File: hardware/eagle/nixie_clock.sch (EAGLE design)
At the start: 67 parts, among them IC1 74141N, IC10 7477N, IC11 74141N, IC12 7477N, IC13 74AC11238, IC2 7477N, IC3 74141N, IC4 7477N, IC5 74141N, IC6 7477N, IC7 74141N, IC8 7477N, IC9 74141N, J1_180V 22-27-2021-02, J1_5V1 22-27-2021-02, J1_5V2 22-27-2021-02, K1 4052, SW1 ROTARTY_ENCODER

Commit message: Working on Sunday
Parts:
- removed Q1: (no value), SparkFun-DiscreteSemi:TRANSISTOR_NPN2N3904
- added C16: 100nF, resistor:C-EU025-024X044
- added D1: LED-RGB-CA-THRUCLEAR, SparkFun-LED:LED-RGB-CA-THRUCLEAR
- added ULN1: (no value), SparkFun-PowerIC:ULN2803DIP
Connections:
- removed net N$124: C1.2, C10.2, C11.2, C12.2, C13.2, C2.2, C3.2, C4.2, C5.2, C6.2, C7.2, C8.2, C9.2, IC10P.VCC, IC11P.VCC, IC12P.VCC, IC13A.G1, IC13P.VCC, IC1P.VCC, IC2P.VCC, IC3P.VCC, IC4P.VCC, IC5P.VCC, IC6P.VCC, IC7P.VCC, IC8P.VCC, IC9P.VCC, J1_5V1-2.S, Q1.C
- new net N$138: GPIO_HEADER1G$1.GPIO$15, ULN1.2
- new net N$139: GPIO_HEADER1G$1.GPIO$16, ULN1.3
- new net N$140: C1.2, C10.2, C11.2, C12.2, C13.2, C16.2, C2.2, C3.2, C4.2, C5.2, C6.2, C7.2, C8.2, C9.2, IC10P.VCC, IC11P.VCC, IC12P.VCC, IC13A.G1, IC13P.VCC, IC1P.VCC, IC2P.VCC, IC3P.VCC, IC4P.VCC, IC5P.VCC, IC6P.VCC, IC7P.VCC, IC8P.VCC, IC9P.VCC, J1_5V1-2.S, ULN1.10
- net GND: now also C16.1, ULN1.9
- net N$137: now also ULN1.1; no longer Q1.B
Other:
- moved on the sheet: SV15, SW1

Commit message: Added uln documentation
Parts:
- removed GPIO_HEADER1: RPI_GPIO_HEADER, rpi-header:RPI_GPIO_HEADER
- added J1: RASPBERRYPI-40-PIN-GPIO, SparkFun-Boards:RASPBERRYPI-40-PIN-GPIO
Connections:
- removed net N$135: GPIO_HEADER1G$1.GPIO$11, SV16.5
- removed net N$136: GPIO_HEADER1G$1.GPIO$13, SV16.3
- new net N$124: J1.CE1, SV16.5
- net N$127: now also J1.MOSI; no longer GPIO_HEADER1G$1.GPIO$12
- net N$129: now also J1.GP4; no longer GPIO_HEADER1G$1.GPIO$7
- net N$130: now also J1.MISO, SV16.3; no longer GPIO_HEADER1G$1.GPIO$10
- net N$137: now also J1.SCLK; no longer GPIO_HEADER1G$1.GPIO$14
- net N$138: now also J1.TXO; no longer GPIO_HEADER1G$1.GPIO$15
- net N$139: now also J1.RXI; no longer GPIO_HEADER1G$1.GPIO$16
- net N$17: now also J1.GP22; no longer GPIO_HEADER1G$1.GPIO$3
- net N$94: now also J1.GP23; no longer GPIO_HEADER1G$1.GPIO$4
- net N$95: now also J1.GP24; no longer GPIO_HEADER1G$1.GPIO$5
- net N$96: now also J1.GP25; no longer GPIO_HEADER1G$1.GPIO$6
- net N$97: now also J1.GP27; no longer GPIO_HEADER1G$1.GPIO$2
- net N$98: now also J1.GP18#; no longer GPIO_HEADER1G$1.GPIO$1
- net N$99: now also J1.GP17; no longer GPIO_HEADER1G$1.GPIO$0
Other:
- moved on the sheet: B1, C1, C10, C11, C12, C13, C14, C15, C16, C2, C3, C4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

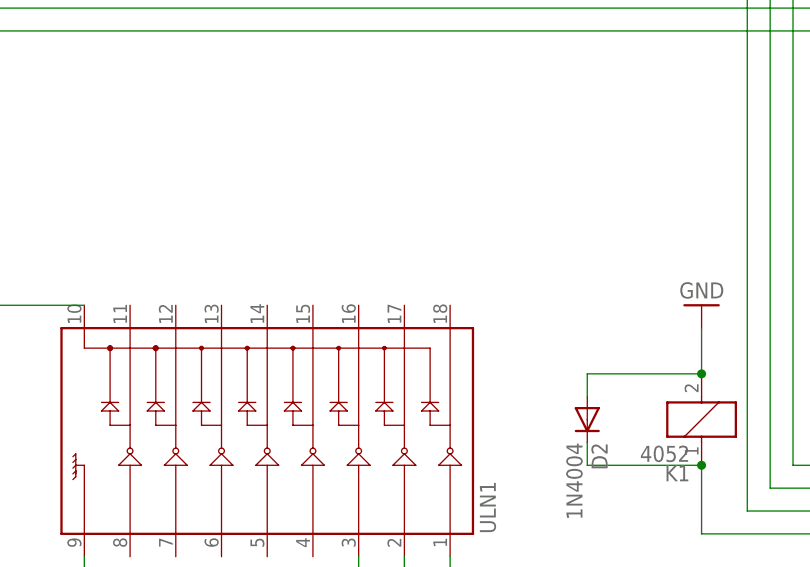
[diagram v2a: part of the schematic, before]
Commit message: Added new model on freecad model and updated pcb board
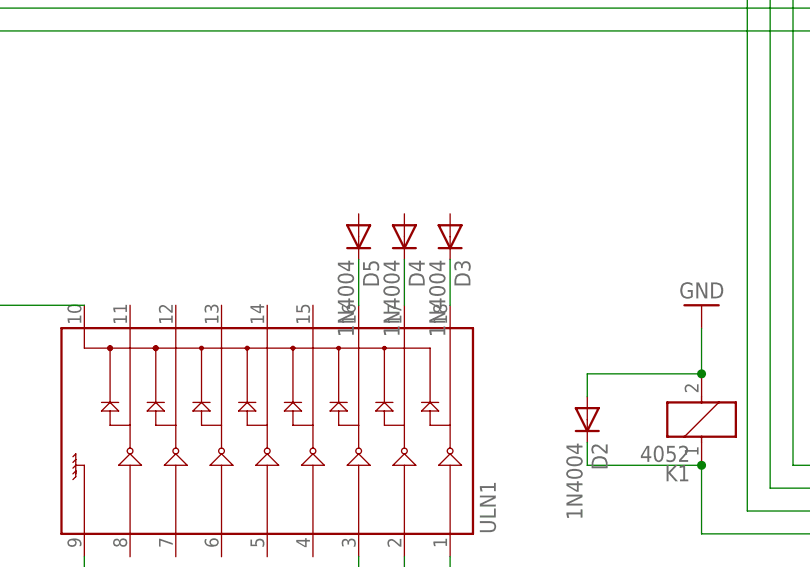
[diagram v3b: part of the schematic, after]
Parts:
- added D3, D4, D5: 1N4004, diode:1N4004
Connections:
- new net N$116: D4.C, ULN1.17
- new net N$135: D3.C, ULN1.18
- new net N$136: D5.C, ULN1.16
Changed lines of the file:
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@@
 </part>
 <part name="J1" library="SparkFun-Boards" deviceset="RASPBERRYPI-40-PIN-GPIO" device=""/>
+<part name="D3" library="diode" deviceset="1N4004" device=""/>
+<part name="D4" library="diode" deviceset="1N4004" device=""/>
+<part name="D5" library="diode" deviceset="1N4004" device=""/>
 </parts>
 <sheets>
@@
 </instance>
 <instance part="J1" gate="G$1" x="368.3" y="111.76"/>
+<instance part="D3" gate="1" x="358.14" y="210.82" rot="R270"/>
+<instance part="D4" gate="1" x="353.06" y="210.82" rot="R270"/>
+<instance part="D5" gate="1" x="347.98" y="210.82" rot="R270"/>
 </instances>
 <busses>
@@
 </segment>
 </net>
+<net name="N$116" class="0">
+<segment>
+<pinref part="D4" gate="1" pin="C"/>
+<pinref part="ULN1" gate="G$1" pin="17"/>
+<wire x1="353.06" y1="208.28" x2="353.06" y2="203.2" width="0.1524" layer="91"/>
+</segment>
+</net>
+<net name="N$135" class="0">
+<segment>
+<pinref part="D3" gate="1" pin="C"/>
+<pinref part="ULN1" gate="G$1" pin="18"/>
+<wire x1="358.14" y1="208.28" x2="358.14" y2="203.2" width="0.1524" layer="91"/>
+</segment>
+</net>
+<net name="N$136" class="0">
+<segment>
+<pinref part="D5" gate="1" pin="C"/>
+<pinref part="ULN1" gate="G$1" pin="16"/>
+<wire x1="347.98" y1="208.28" x2="347.98" y2="203.2" width="0.1524" layer="91"/>
+</segment>
+</net>

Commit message: Updated project: new documentation & more ...
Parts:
- removed IC13: 74AC11238, 74ac-logic:74AC11238
- added U$1: M74HC238, SparkFun-DigitalIC:M74HC238
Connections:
- net GND: now also C13.2, U$1.GND, U$1.~G2A, U$1.~G2B; no longer C13.1, IC13A.G2A, IC13A.G2B, IC13P.GND
- net N$140: now also C13.1, U$1.G1, U$1.VCC; no longer C13.2, IC13A.G1, IC13P.VCC
- net N$16: now also U$1.Y0; no longer IC13A.Y0
- net N$33: now also U$1.Y1; no longer IC13A.Y1
- net N$48: now also U$1.Y2; no longer IC13A.Y2
- net N$63: now also U$1.Y3; no longer IC13A.Y3
- net N$78: now also U$1.Y4; no longer IC13A.Y4
- net N$93: now also U$1.Y5; no longer IC13A.Y5
- net N$97: now also U$1.A; no longer IC13A.A
- net N$98: now also U$1.B; no longer IC13A.B
- net N$99: now also U$1.C; no longer IC13A.C
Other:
- moved on the sheet: C13

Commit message: Fixed some issues related with the multiplexed data
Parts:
- removed U$1: M74HC238, SparkFun-DigitalIC:M74HC238
- added C17: 100nF, resistor:C-EU025-024X044
- added C18: 1uF, rcl:CPOL-EUE2.5-5
- added IC13: 74HCT259N, 74xx-eu:74HCT259N
- added IC15: 7477N, 74xx-eu:7477N
- added R7: 10k, rcl:R-EU_0204/7
- added R8: 4k7, rcl:R-EU_0204/7
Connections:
- removed net N$139: J1.RXI, ULN1.3
- new net N$141: IC15A.1D, J1.GP25
- new net N$142: IC15A.2D, J1.GP24
- new net N$143: IC15A.3D, J1.GP23
- new net N$144: IC15A.4D, J1.GP22
- new net N$145: C1.2, C10.2, C11.2, C12.2, C13.2, C16.2, C17.2, C2.2, C3.2, C4.2, C5.2, C6.2, C7.2, C8.2, C9.2, IC10P.VCC, IC11P.VCC, IC12P.VCC, IC13A.D, IC13P.VCC, IC15P.VCC, IC1P.VCC, IC2P.VCC, IC3P.VCC, IC4P.VCC, IC5P.VCC, IC6P.VCC, IC7P.VCC, IC8P.VCC, IC9P.VCC, J1_5V1-2.S, R7.2, R8.1, SV16.1, ULN1.10
- new net N$146: IC15A.12C, IC15A.34C, J1.GP4, ULN1.4
- new net N$149: D2.C, J1.GP20, K11.1
- net GND: now also C13.1, C17.1, C18.-, IC13P.GND, IC15P.GND, SV16.2; no longer C13.2, U$1.GND, U$1.~G2A, U$1.~G2B
- net N$124: now also J1.GP19, ULN1.1; no longer J1.CE1, SV16.5
- net N$127: now also J1.GP26, ULN1.2; no longer J1.MOSI, SV16.4
- net N$129: now also J1.GP12, ULN1.3; no longer D2.C, J1.GP4, K11.1
- net N$130: now also C18.+, J1.GP13, R8.2; no longer J1.MISO
- net N$137: now also J1.GP6, SV16.5; no longer J1.SCLK, ULN1.1
- net N$138: now also J1.GP5, SV16.4; no longer J1.TXO, ULN1.2
- net N$140: now also IC13A.CLR, IC13A.G, R7.1, ULN1.15; no longer C1.2, C10.2, C11.2, C12.2, C13.1, C16.2, C2.2, C3.2, C4.2, C5.2, C6.2, C7.2, C8.2, C9.2, IC10P.VCC, IC11P.VCC, IC12P.VCC, IC1P.VCC, IC2P.VCC, IC3P.VCC, IC4P.VCC, IC5P.VCC, IC6P.VCC, IC7P.VCC, IC8P.VCC, IC9P.VCC, J1_5V1-2.S, U$1.G1, U$1.VCC, ULN1.10
- net N$16: now also IC13A.Q0; no longer U$1.Y0
- net N$17: now also IC15A.4Q; no longer J1.GP22
- net N$33: now also IC13A.Q1; no longer U$1.Y1
- net N$48: now also IC13A.Q2; no longer U$1.Y2
- net N$63: now also IC13A.Q3; no longer U$1.Y3
- net N$78: now also IC13A.Q4; no longer U$1.Y4
- net N$93: now also IC13A.Q5; no longer U$1.Y5
- net N$94: now also IC15A.3Q; no longer J1.GP23
- net N$95: now also IC15A.2Q; no longer J1.GP24
- net N$96: now also IC15A.1Q; no longer J1.GP25
- net N$97: now also IC13A.S0; no longer U$1.A
- net N$98: now also IC13A.S1; no longer U$1.B
- net N$99: now also IC13A.S2; no longer U$1.C
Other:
- moved on the sheet: C13, C16, D2, D3, D4, D5, J1, K1, SV15, SV16, SW1, ULN1

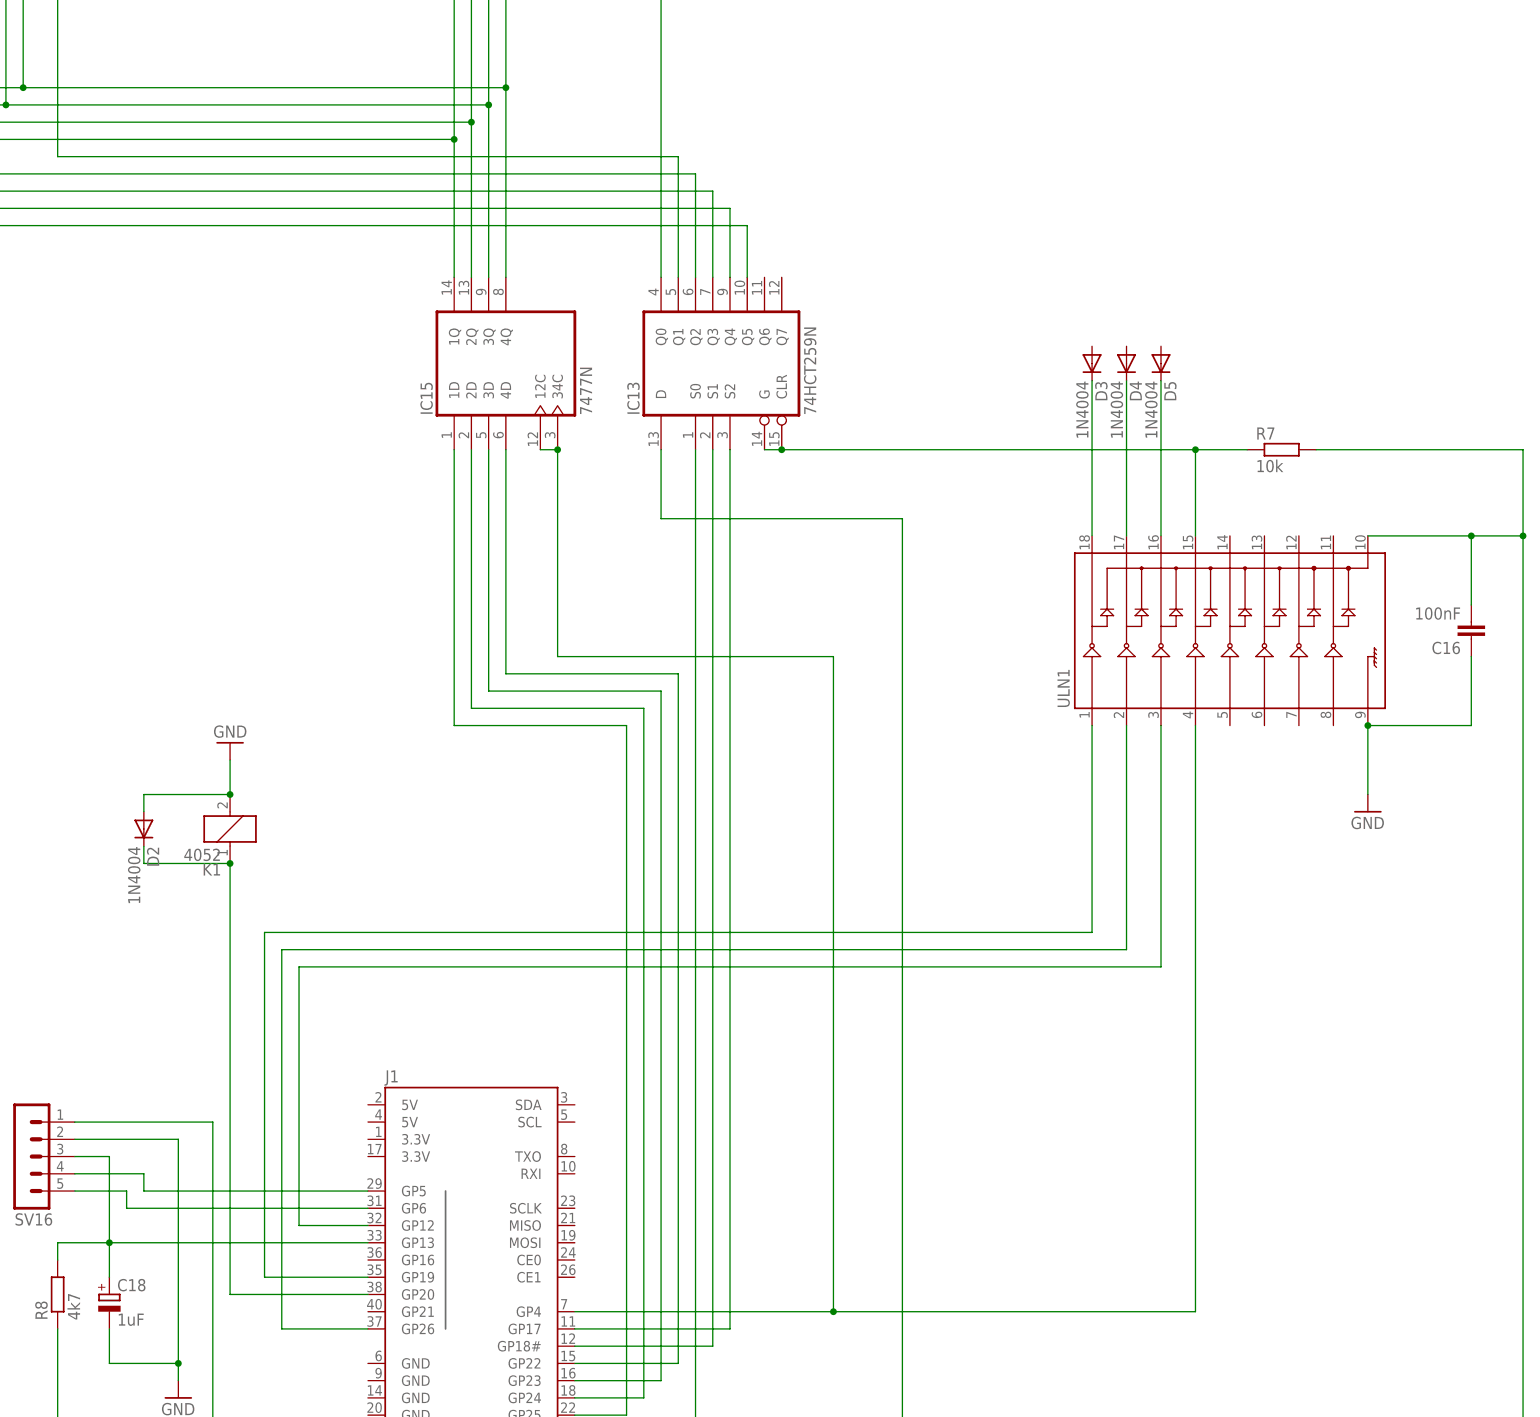
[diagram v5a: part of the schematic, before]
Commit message: Updated clock.c and removed rencoder test
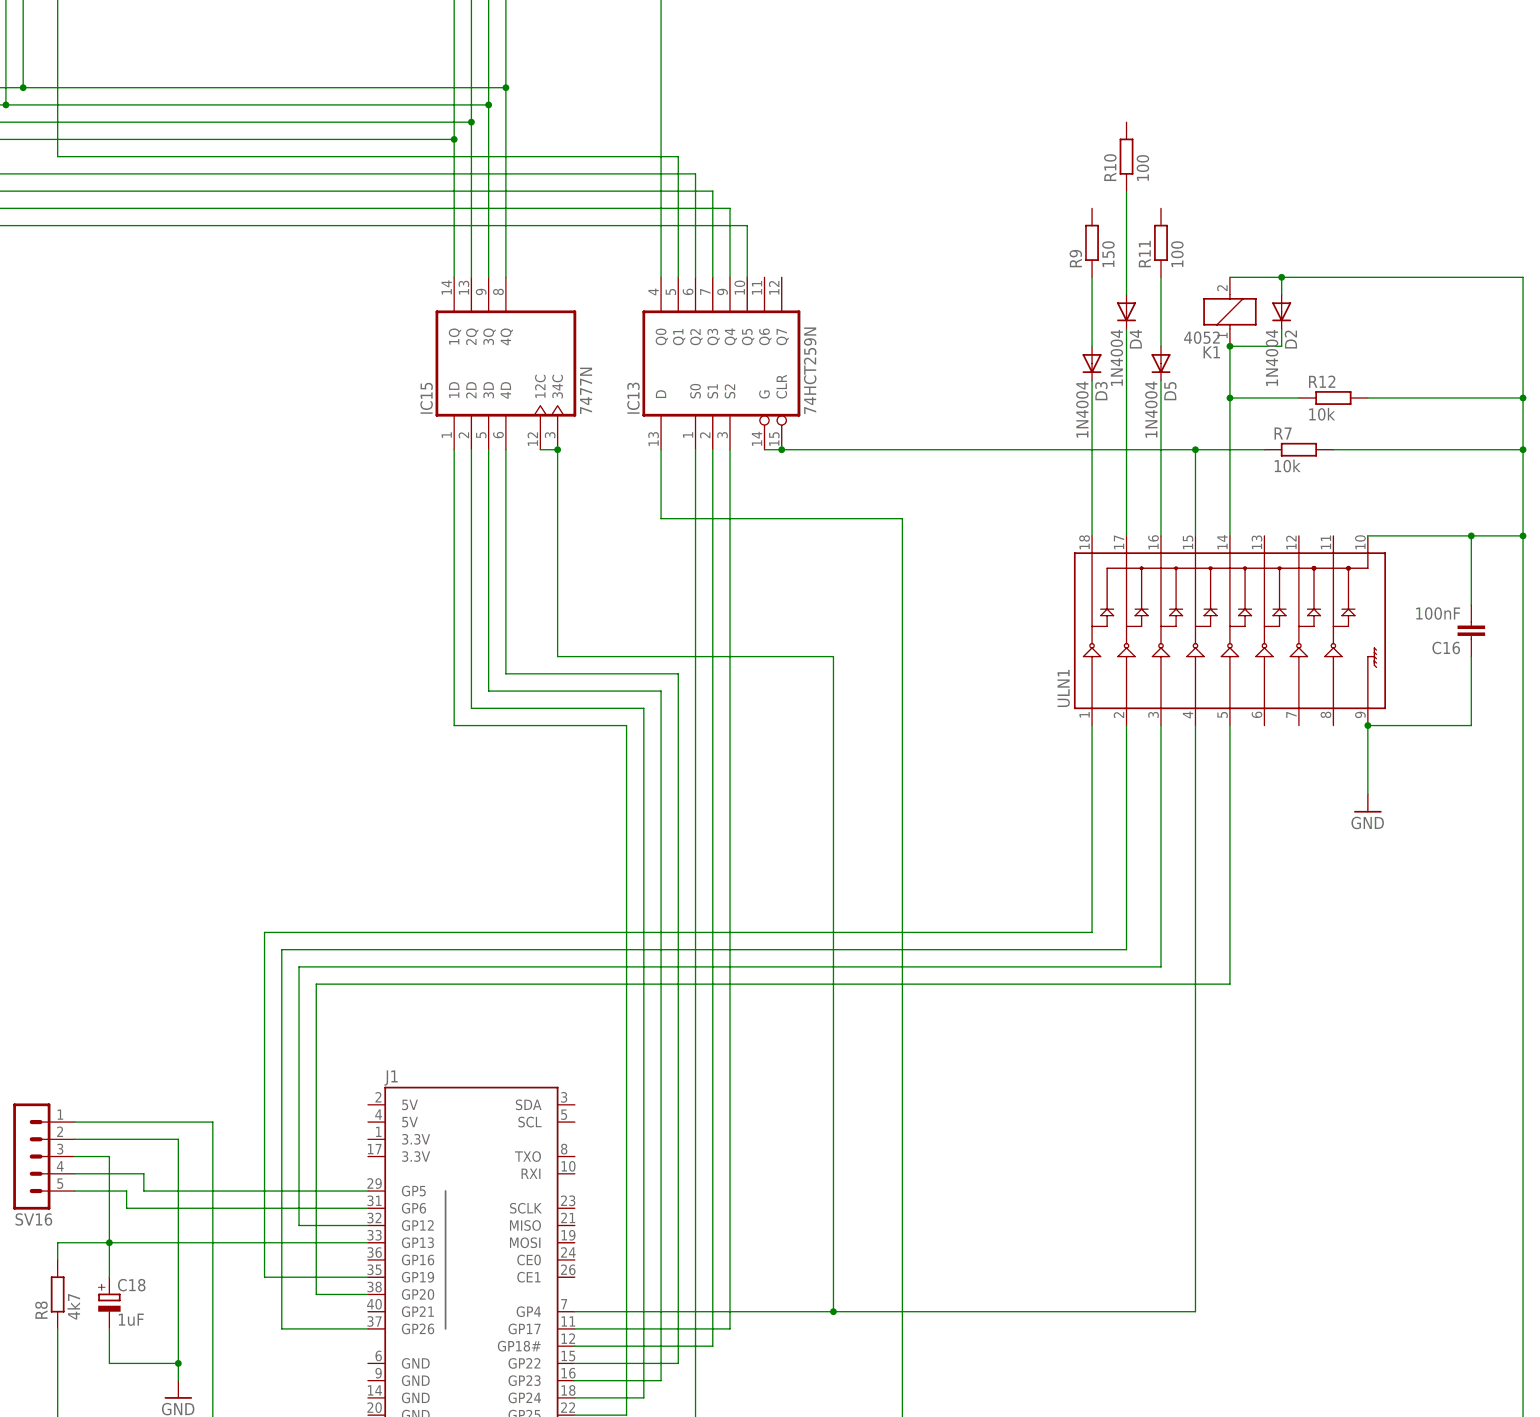
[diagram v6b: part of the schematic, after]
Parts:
- added R10, R11: 100, rcl:R-EU_0204/7
- added R12: 10k, rcl:R-EU_0204/7
- added R9: 150, rcl:R-EU_0204/7
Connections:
- removed net N$145: C1.2, C10.2, C11.2, C12.2, C13.2, C16.2, C17.2, C2.2, C3.2, C4.2, C5.2, C6.2, C7.2, C8.2, C9.2, IC10P.VCC, IC11P.VCC, IC12P.VCC, IC13A.D, IC13P.VCC, IC15P.VCC, IC1P.VCC, IC2P.VCC, IC3P.VCC, IC4P.VCC, IC5P.VCC, IC6P.VCC, IC7P.VCC, IC8P.VCC, IC9P.VCC, J1_5V1-2.S, R7.2, R8.1, SV16.1, ULN1.10
- new net N$139: D3.A, R9.1
- new net N$147: D4.A, R10.1
- new net N$148: D5.A, R11.1
- new net N$151: D2.C, K11.1, R12.1, ULN1.14
- new net N$152: C1.2, C10.2, C11.2, C12.2, C13.2, C16.2, C17.2, C2.2, C3.2, C4.2, C5.2, C6.2, C7.2, C8.2, C9.2, D2.A, IC10P.VCC, IC11P.VCC, IC12P.VCC, IC13A.D, IC13P.VCC, IC15P.VCC, IC1P.VCC, IC2P.VCC, IC3P.VCC, IC4P.VCC, IC5P.VCC, IC6P.VCC, IC7P.VCC, IC8P.VCC, IC9P.VCC, J1_5V1-2.S, K11.2, R12.2, R7.2, R8.1, SV16.1, ULN1.10
- net GND: no longer D2.A, K11.2
- net N$149: now also ULN1.5; no longer D2.C, K11.1
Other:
- moved on the sheet: D2, D4, K1, R7
